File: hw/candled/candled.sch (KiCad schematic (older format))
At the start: 10 parts, among them J1 Power, J2 HC-05, J3 ISP-6, U1 ATtiny85-20PU

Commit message: comment on design
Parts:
- added R4: 1K, symbol Device:R
- added R5: 2K, symbol Device:R
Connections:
- net EN is gone; now on net GND: J2.6 (Pin_6)
- net GND: now also R5.2
- net PB0: now also R4.1; no longer J2.2 (Pin_2)
- new net RX: J2.2 (Pin_2), R4.2, R5.1
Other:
- note added: "HC-05/06 notes\n\n1. KEY/En \n This pin is used to bring the Bluetooth module in AT commands mode. \n The Key/EN pin should be high to operate Bluetooth in command mode.\n Default baud speed in command mode is 38400bps and 9600 in data mode (default mode).\n2. VCC \n Used to power the Bluetooth module. Give 5V / 3.3 V to this Pin.\n3. GND \n The ground pin of the module\n4. TXD \n Connect this pi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"
- note removed: "HC-05 notes\n\n1. KEY/En \n This pin is used to bring the Bluetooth module in AT commands mode. \n The Key/EN pin should be high to operate Bluetooth in command mode.\n Default baud speed in command mode is 38400bps and 9600 in data mode (default mode).\n2. VCC \n Used to power the Bluetooth module. Give 5V / 3.3 V to this Pin.\n3. GND \n The ground pin of the module\n4. TXD \n Connect this pin w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"
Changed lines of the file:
@@
 Wire Wire Line
 	3600 4300 3950 4300
-Wire Wire Line
-	3950 4300 3950 4900
 $Comp
 L power:GND #PWR02
 U 1 1 6156F570
-P 3950 4900
-F 0 "#PWR02" H 3950 4650 50  0001 C CNN
-F 1 "GND" H 3955 4727 50  0000 C CNN
-F 2 "" H 3950 4900 50  0001 C CNN
-F 3 "" H 3950 4900 50  0001 C CNN
-	1    3950 4900
+P 3950 5050
+F 0 "#PWR02" H 3950 4800 50  0001 C CNN
+F 1 "GND" H 3955 4877 50  0000 C CNN
+F 2 "" H 3950 5050 50  0001 C CNN
+F 3 "" H 3950 5050 50  0001 C CNN
+	1    3950 5050
 	1    0    0    -1
 $EndComp
@@
 Wire Wire Line
 	5550 2350 5550 2750
-Wire Wire Line
-	5550 3950 5550 4900
 $Comp
 L power:GND #PWR03
 U 1 1 6157018C
-P 5550 4900
-F 0 "#PWR03" H 5550 4650 50  0001 C CNN
-F 1 "GND" H 5555 4727 50  0000 C CNN
-F 2 "" H 5550 4900 50  0001 C CNN
-F 3 "" H 5550 4900 50  0001 C CNN
-	1    5550 4900
+P 5550 5050
+F 0 "#PWR03" H 5550 4800 50  0001 C CNN
+F 1 "GND" H 5555 4877 50  0000 C CNN
+F 2 "" H 5550 5050 50  0001 C CNN
+F 3 "" H 5550 5050 50  0001 C CNN
+	1    5550 5050
 	1    0    0    -1
 $EndComp
@@
 $EndSheet
 Wire Wire Line
-	6150 3050 6650 3050
-Wire Wire Line
 	7100 2300 7100 3150
-Wire Wire Line
-	7100 3150 6500 3150
 Wire Wire Line
 	6900 2300 6900 3250
@@
 Wire Wire Line
 	8200 3450 8200 3900
-Wire Wire Line
-	3600 4400 6500 4400
-Wire Wire Line
-	6500 4400 6500 3150
-Connection ~ 6500 3150
-Wire Wire Line
-	6500 3150 6150 3150
-Wire Wire Line
-	3600 4500 6650 4500
-Wire Wire Line
-	6650 4500 6650 3050
-Connection ~ 6650 3050
-Wire Wire Line
-	6650 3050 7000 3050
 Text Notes 8250 3350 0    43   ~ 0
 Might not be possible to have 3 PWM controlled LEDs together with \nserial comms with BLE module\n
-Text Notes 3850 4200 0    43   ~ 0
+Text Notes 4000 4250 0    43   ~ 0
 custom serial comms using hardware USI\nmight require external crystal for exact timing
-Text Notes 4300 4650 0    43   ~ 0
+Text Notes 6700 3850 0    43   ~ 0
 RX is operating on 3.3V\nneeds voltage divider!
 Text Notes 650  5600 0    43   ~ 0
-HC-05 notes\n\n1. KEY/En \n This pin is used to bring the Bluetooth module in AT commands mode. \n The Key/EN pin should be high to operate Bluetooth in command mode.\n Default baud speed in command mode is 38400bps and 9600 in data mode (default mode).\n2. VCC \n Used to power the Bluetooth module. Give 5V / 3.3 V to this Pin.\n3. GND \n The ground pin of the module\n4. TXD \n Connect this pin with the RXD pin of the Microcontroller.\n5. RXD \n Connect this pin to the TXD pin of the Microcontroller.\n6. STATE \n Used to check if the module is connected or not. It acts as a status indicator.
+HC-05/06 notes\n\n1. KEY/En \n This pin is used to bring the Bluetooth module in AT commands mode. \n The Key/EN pin should be high to operate Bluetooth in command mode.\n Default baud speed in command mode is 38400bps and 9600 in data mode (default mode).\n2. VCC \n Used to power the Bluetooth module. Give 5V / 3.3 V to this Pin.\n3. GND \n The ground pin of the module\n4. TXD \n Connect this pin with the RXD pin of the Microcontroller.\n5. RXD \n Connect this pin to the TXD pin of the Microcontroller.\n6. STATE \n Used to check if the module is connected or not. It acts as a status indicator.
+Wire Wire Line
+	3600 4200 3950 4200
+Wire Wire Line
+	3950 4200 3950 2350
+$Comp
+L Device:R R5
+U 1 1 61582D36
+P 6650 4550
+F 0 "R5" H 6720 4596 50  0000 L CNN
+F 1 "2K" H 6720 4505 50  0000 L CNN
+F 2 "" V 6580 4550 50  0001 C CNN
+F 3 "~" H 6650 4550 50  0001 C CNN
+	1    6650 4550
+	1    0    0    -1
+$EndComp
+$Comp
+L Device:R R4
+U 1 1 615843D2
+P 6650 4050
+F 0 "R4" H 6720 4096 50  0000 L CNN
+F 1 "1K" H 6720 4005 50  0000 L CNN
+F 2 "" V 6580 4050 50  0001 C CNN
+F 3 "~" H 6650 4050 50  0001 C CNN
+	1    6650 4050
+	1    0    0    -1
+$EndComp
+$Comp
+L power:GND #PWR014
+U 1 1 61584968
+P 6650 5050
+F 0 "#PWR014" H 6650 4800 50  0001 C CNN
+F 1 "GND" H 6655 4877 50  0000 C CNN
+F 2 "" H 6650 5050 50  0001 C CNN
+F 3 "" H 6650 5050 50  0001 C CNN
+	1    6650 5050
+	1    0    0    -1
+$EndComp
+Wire Wire Line
+	3950 4300 3950 5050
+Wire Wire Line
+	5550 3950 5550 5050
+Wire Wire Line
+	6650 4700 6650 5050
+Wire Wire Line
+	6150 3050 6650 3050
+Wire Wire Line
+	3600 4400 6350 4400
+Wire Wire Line
+	6350 3150 6350 4400
+Connection ~ 6350 3150
+Wire Wire Line
+	6350 3150 6150 3150
+Wire Wire Line
+	6350 3150 7100 3150
+Wire Wire Line
+	3600 4500 6500 4500
+Wire Wire Line
+	6500 4500 6500 4300
+Wire Wire Line
+	6500 4300 6650 4300
+Wire Wire Line
+	6650 4300 6650 4200
+Wire Wire Line
+	6650 4300 6650 4400
+Connection ~ 6650 4300
+Wire Wire Line
+	6650 3900 6650 3050
+Connection ~ 6650 3050
+Wire Wire Line
+	6650 3050 7000 3050
+Wire Wire Line
+	3600 2450 3850 2450
+Wire Wire Line
+	3850 2450 3850 4100
+Wire Wire Line
+	3850 4100 3600 4100
+Connection ~ 3600 2450
 $EndSCHEMATC

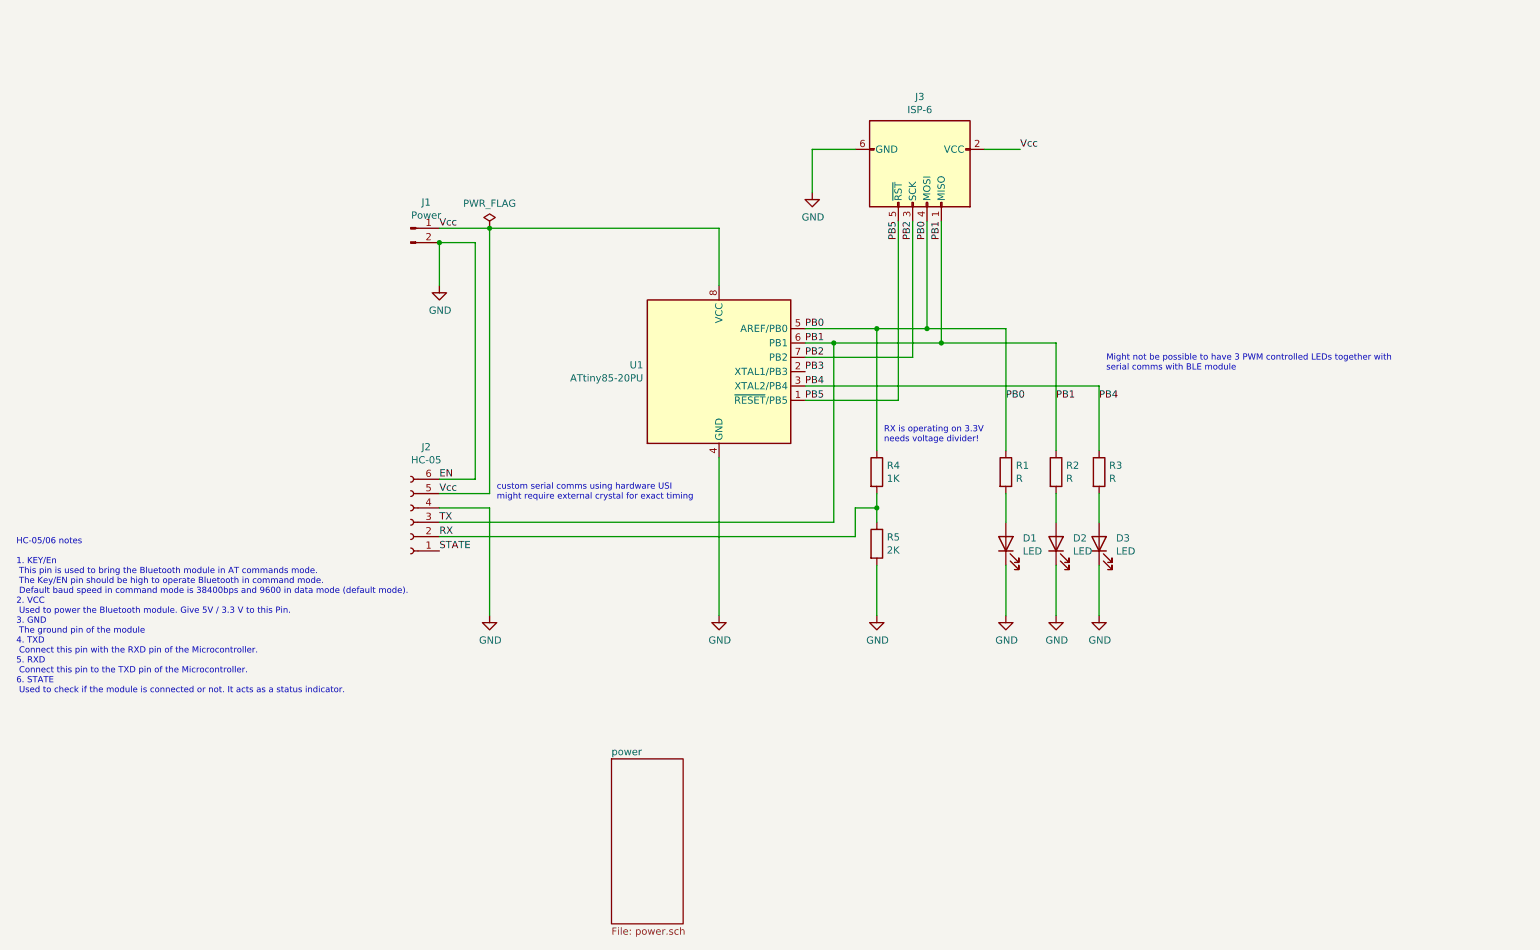
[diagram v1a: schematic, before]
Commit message: add one-pin TX/RX schematic design
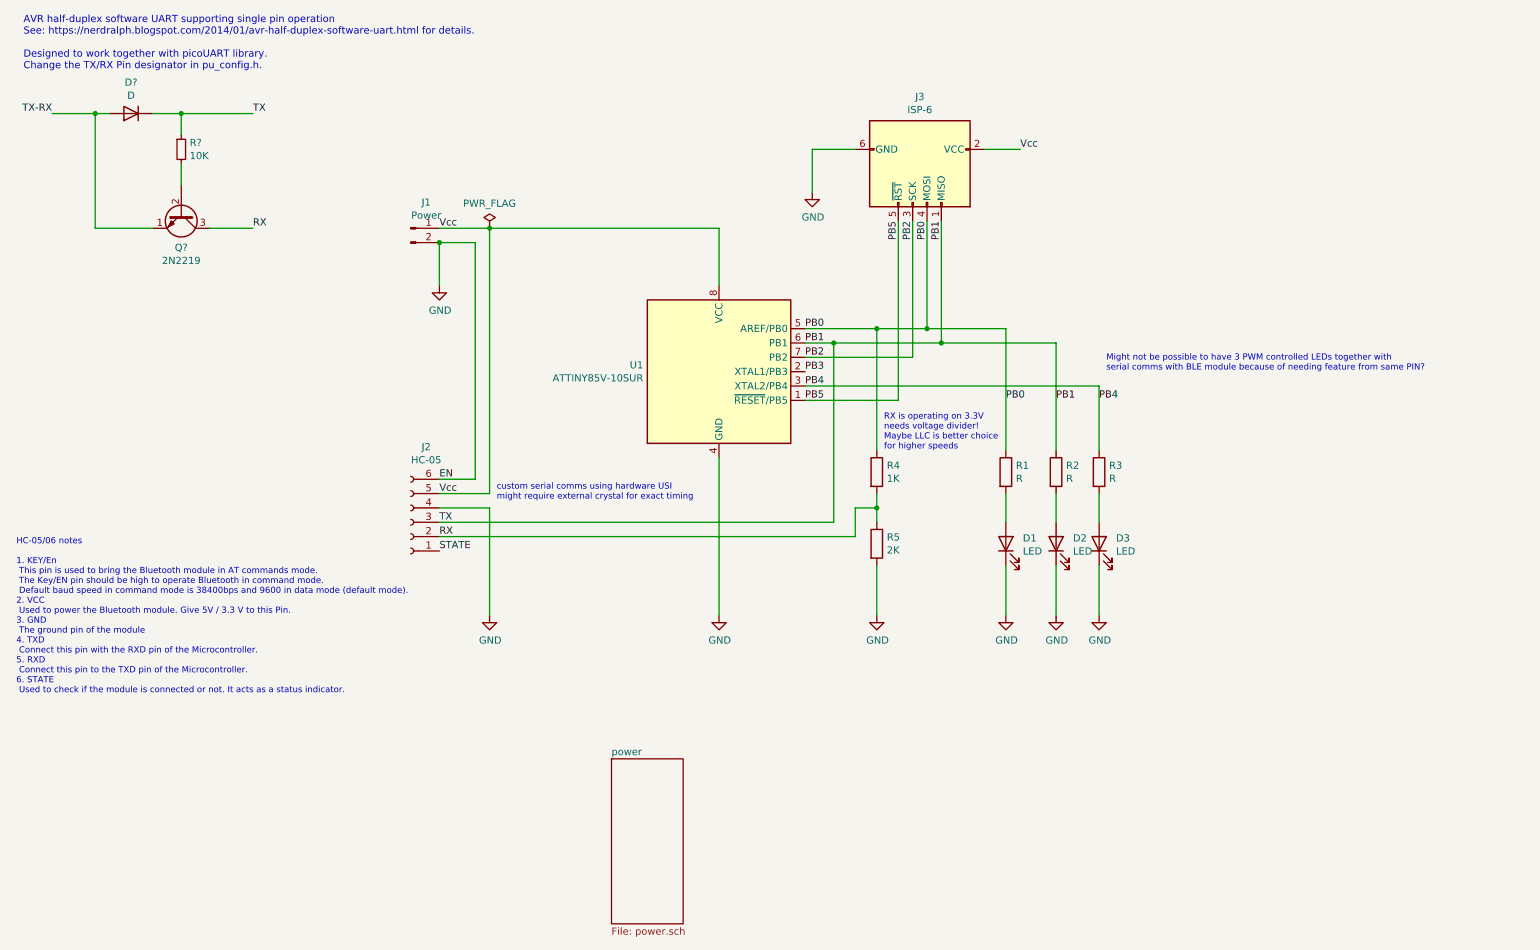
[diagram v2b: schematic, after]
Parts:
- added D?: D, symbol Device:D
- added Q?: 2N2219, Package_TO_SOT_THT:TO-39-3, symbol Transistor_BJT:2N2219
- added R?: 10K, symbol Device:R_Small
- U1: value ATtiny85-20PU -> ATTINY85V-10SUR
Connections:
- net PB1: now also D?.1 (K), R?.1
- net RX: now also Q?.3 (C)
- new net: Q?.2 (B), R?.2
- new net TX-RX: D?.2 (A), Q?.1 (E)
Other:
- note added: "AVR half-duplex software UART supporting single pin operation\nSee: https://nerdralph.blogspot.com/2014/01/avr-half-duplex-software-uart.html for details.\n\nDesigned to work together with picoUART library.\nChange the TX/RX Pin designator in pu_config.h."
- note added: "Might not be possible to have 3 PWM controlled LEDs together with \nserial comms with BLE module because of needing feature from same PIN?\n"
- note added: "RX is operating on 3.3V\nneeds voltage divider!\nMaybe LLC is better choice \nfor higher speeds"
- note removed: "Might not be possible to have 3 PWM controlled LEDs together with \nserial comms with BLE module\n"
- note removed: "RX is operating on 3.3V\nneeds voltage divider!"
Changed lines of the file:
@@
 P 5550 3350
 F 0 "U1" H 5021 3396 50  0000 R CNN
-F 1 "ATtiny85-20PU" H 5021 3305 50  0000 R CNN
+F 1 "ATTINY85V-10SUR" H 5021 3305 50  0000 R CNN
 F 2 "Package_DIP:DIP-8_W7.62mm" H 5550 3350 50  0001 C CIN
 F 3 "http://ww1.microchip.com/downloads/en/DeviceDoc/atmel-2586-avr-8-bit-microcontroller-attiny25-attiny45-attiny85_datasheet.pdf" H 5550 3350 50  0001 C CNN
@@
 	8200 3450 8200 3900
 Text Notes 8250 3350 0    43   ~ 0
-Might not be possible to have 3 PWM controlled LEDs together with \nserial comms with BLE module\n
+Might not be possible to have 3 PWM controlled LEDs together with \nserial comms with BLE module because of needing feature from same PIN?\n
 Text Notes 4000 4250 0    43   ~ 0
 custom serial comms using hardware USI\nmight require external crystal for exact timing
-Text Notes 6700 3850 0    43   ~ 0
-RX is operating on 3.3V\nneeds voltage divider!
+Text Notes 6700 3900 0    43   ~ 0
+RX is operating on 3.3V\nneeds voltage divider!\nMaybe LLC is better choice \nfor higher speeds
 Text Notes 650  5600 0    43   ~ 0
 HC-05/06 notes\n\n1. KEY/En \n This pin is used to bring the Bluetooth module in AT commands mode. \n The Key/EN pin should be high to operate Bluetooth in command mode.\n Default baud speed in command mode is 38400bps and 9600 in data mode (default mode).\n2. VCC \n Used to power the Bluetooth module. Give 5V / 3.3 V to this Pin.\n3. GND \n The ground pin of the module\n4. TXD \n Connect this pin with the RXD pin of the Microcontroller.\n5. RXD \n Connect this pin to the TXD pin of the Microcontroller.\n6. STATE \n Used to check if the module is connected or not. It acts as a status indicator.
@@
 	3850 4100 3600 4100
 Connection ~ 3600 2450
+$Comp
+L Device:D D?
+U 1 1 616C288A
+P 1450 1550
+F 0 "D?" H 1450 1333 50  0000 C CNN
+F 1 "D" H 1450 1424 50  0000 C CNN
+F 2 "" H 1450 1550 50  0001 C CNN
+F 3 "~" H 1450 1550 50  0001 C CNN
+	1    1450 1550
+	-1   0    0    1
+$EndComp
+$Comp
+L Device:R_Small R?
+U 1 1 616C3591
+P 1800 1800
+F 0 "R?" H 1859 1846 50  0000 L CNN
+F 1 "10K" H 1859 1755 50  0000 L CNN
+F 2 "" H 1800 1800 50  0001 C CNN
+F 3 "~" H 1800 1800 50  0001 C CNN
+	1    1800 1800
+	1    0    0    -1
+$EndComp
+$Comp
+L Transistor_BJT:2N2219 Q?
+U 1 1 616C5D37
+P 1800 2250
+F 0 "Q?" V 2035 2250 50  0000 C CNN
+F 1 "2N2219" V 2126 2250 50  0000 C CNN
+F 2 "Package_TO_SOT_THT:TO-39-3" H 2000 2175 50  0001 L CIN
+F 3 "http://www.onsemi.com/pub_link/Collateral/2N2219-D.PDF" H 1800 2250 50  0001 L CNN
+	1    1800 2250
+	0    1    1    0
+$EndComp
+Wire Wire Line
+	1300 1550 1200 1550
+Wire Wire Line
+	1600 2350 1200 2350
+Wire Wire Line
+	1200 2350 1200 1550
+Connection ~ 1200 1550
+Wire Wire Line
+	1200 1550 900  1550
+Wire Wire Line
+	1600 1550 1800 1550
+Wire Wire Line
+	1800 1700 1800 1550
+Connection ~ 1800 1550
+Wire Wire Line
+	1800 1550 2300 1550
+Wire Wire Line
+	1800 1900 1800 2050
+Wire Wire Line
+	2000 2350 2300 2350
+Text Label 900  1550 2    50   ~ 0
+TX-RX
+Text Label 2300 1550 0    50   ~ 0
+TX
+Text Label 2300 2350 0    50   ~ 0
+RX
+Text Notes 700  1250 0    50   ~ 0
+AVR half-duplex software UART supporting single pin operation\nSee: https://nerdralph.blogspot.com/2014/01/avr-half-duplex-software-uart.html for details.\n\nDesigned to work together with picoUART library.\nChange the TX/RX Pin designator in pu_config.h.
 $EndSCHEMATC

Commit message: one-wire UART R&D
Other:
- note added: "hm-xx"
- note added: "micro"
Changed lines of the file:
@@
 Text Notes 700  1250 0    50   ~ 0
 AVR half-duplex software UART supporting single pin operation\nSee: https://nerdralph.blogspot.com/2014/01/avr-half-duplex-software-uart.html for details.\n\nDesigned to work together with picoUART library.\nChange the TX/RX Pin designator in pu_config.h.
+Text Notes 700  1950 0    50   ~ 0
+micro
+Text Notes 2400 1950 0    50   ~ 0
+hm-xx
 $EndSCHEMATC

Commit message: minor changes
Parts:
- Q?: value 2N2219 -> BC547
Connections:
- net TX-RX is gone; now on net PB3: D?.2 (A), Q?.1 (E)
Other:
- note added: "AVR half-duplex software UART supporting single pin operation\nSee: https://nerdralph.blogspot.com/2014/01/avr-half-duplex-software-uart.html for details.\n\nDesigned to work together with picoUART library.\nChange the TX/RX Pin designator (PB3) in pu_config.h.\n"
- note added: "HM-10"
- note removed: "AVR half-duplex software UART supporting single pin operation\nSee: https://nerdralph.blogspot.com/2014/01/avr-half-duplex-software-uart.html for details.\n\nDesigned to work together with picoUART library.\nChange the TX/RX Pin designator in pu_config.h."
- note removed: "hm-xx"
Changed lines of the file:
@@
 P 1800 2250
 F 0 "Q?" V 2035 2250 50  0000 C CNN
-F 1 "2N2219" V 2126 2250 50  0000 C CNN
+F 1 "BC547" V 2126 2250 50  0000 C CNN
 F 2 "Package_TO_SOT_THT:TO-39-3" H 2000 2175 50  0001 L CIN
 F 3 "http://www.onsemi.com/pub_link/Collateral/2N2219-D.PDF" H 1800 2250 50  0001 L CNN
@@
 Wire Wire Line
 	2000 2350 2300 2350
-Text Label 900  1550 2    50   ~ 0
-TX-RX
 Text Label 2300 1550 0    50   ~ 0
 TX
@@
 RX
 Text Notes 700  1250 0    50   ~ 0
-AVR half-duplex software UART supporting single pin operation\nSee: https://nerdralph.blogspot.com/2014/01/avr-half-duplex-software-uart.html for details.\n\nDesigned to work together with picoUART library.\nChange the TX/RX Pin designator in pu_config.h.
+AVR half-duplex software UART supporting single pin operation\nSee: https://nerdralph.blogspot.com/2014/01/avr-half-duplex-software-uart.html for details.\n\nDesigned to work together with picoUART library.\nChange the TX/RX Pin designator (PB3) in pu_config.h.\n
 Text Notes 700  1950 0    50   ~ 0
 micro
 Text Notes 2400 1950 0    50   ~ 0
-hm-xx
+HM-10
+Text Label 900  1550 2    50   ~ 0
+PB3
 $EndSCHEMATC
